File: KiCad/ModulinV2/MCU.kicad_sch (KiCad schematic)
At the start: 36 parts, among them IC1 STM32F401VET6, IC2 STM32F401RET6, J1 USB4105-GF-A, Q1 BC847B,215, Q2 BC847B,215, Q3 BC847B,215, SW1 SW_Push, SW2 SW_Push

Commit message: Added initial power supply schematic and modified MCU components
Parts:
- removed IC1: STM32F401VET6, Modulin:QFP50P1600X1600X160-100N, symbol STM32F401VET6:STM32F401VET6
- removed LED1: 150060VS75000, LEDC1608X80N, symbol 150060VS75000:150060VS75000
- removed Q1, Q2, Q3: BC847B,215, BC847B215, symbol BC847B_215:BC847B,215
- removed R4, R6, R9: 68k, symbol Device:R
- added C83, C84, C85: 100n, symbol Device:C
- added IC31: USBLC6-2SC6, SOT95P280X145-6N, symbol USBLC6-2SC6:USBLC6-2SC6
- added J3: TSW-104-07-G-S, TSW10407GS, symbol TSW-104-07-G-S:TSW-104-07-G-S
- added J4: TSM-103-01-T-DV, TSM-103-YY-ZZZ-DV, symbol TSM-103-01-T-DV:TSM-103-01-T-DV
- added JP5: OLED_PWR, symbol Jumper:SolderJumper_3_Open
- added R118, R119: 10k, symbol Device:R
- added S2: PEC12R-3220F-S0024, PEC12R3220FS0024, symbol PEC12R-3220F-S0024:PEC12R-3220F-S0024
- R3: value 300 -> 10k
- R5: value 130 -> 240
- R7, R8: value 51 -> 240
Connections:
- net ADSR_ENC_A is gone; now on net ENC_A: IC2.14 (PA0)
- net +3.3V: now also R3.1, J4.3, JP5.1 (A), R118.2, S2.2
- net +5V: now also JP5.3 (B)
- net GND: now also C83.2, C84.2, C85.2, IC31.2, J3.1, J4.1, R119.2, S2.C1 (COM), S2.MH1, S2.MH2
- net LED_B: now also R8.2
- net LED_G: now also R7.1
- net LED_R: now also R5.2
- net NRST: now also J4.2
- net SCL: now also J3.3
- net SDA: now also J3.4
- net SWCLK: now also J4.4
- net SWDIO: now also J4.6
- net SWO: now also J4.5
- net USB_DM: now also IC31.1, IC31.6
- net USB_DP: now also IC31.3, IC31.4
- net VBUS: now reaches D1.2 (A), J1.A4 (VBUS), J1.A9 (VBUS), J1.B4 (VBUS), J1.B9 (VBUS)
- net VBUS: now also C83.1, IC31.5; no longer R3.1
- net ENC_A: now reaches R3.2
- net ENC_A: now also C84.1, S2.A1 (CH_A)
- net at R8.1: now also LED2.2
- net at LED2.3: now also R7.2; no longer R7.1
- net ENC_SW: now reaches IC2.16 (PA2)
- net ENC_SW: now also R119.1, S2.1
- net ADSR_ENC_B renamed ENC_B
- net ENC_B: now also C85.1, R118.1, S2.B1 (CH_B)
- net LFO_ENC_A: no longer names the net of IC2.41 (PA8)
- net LFO_ENC_B: no longer names the net of IC2.42 (PA9)
- new net: J3.2, JP5.2 (C)
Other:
- note added: "Debug LED and OLED"
- note added: "Debugger interface"
- note added: "USB interface"
- moved on the sheet: D1, IC2, J1, LED2, R1, R2, R5, R7, R8

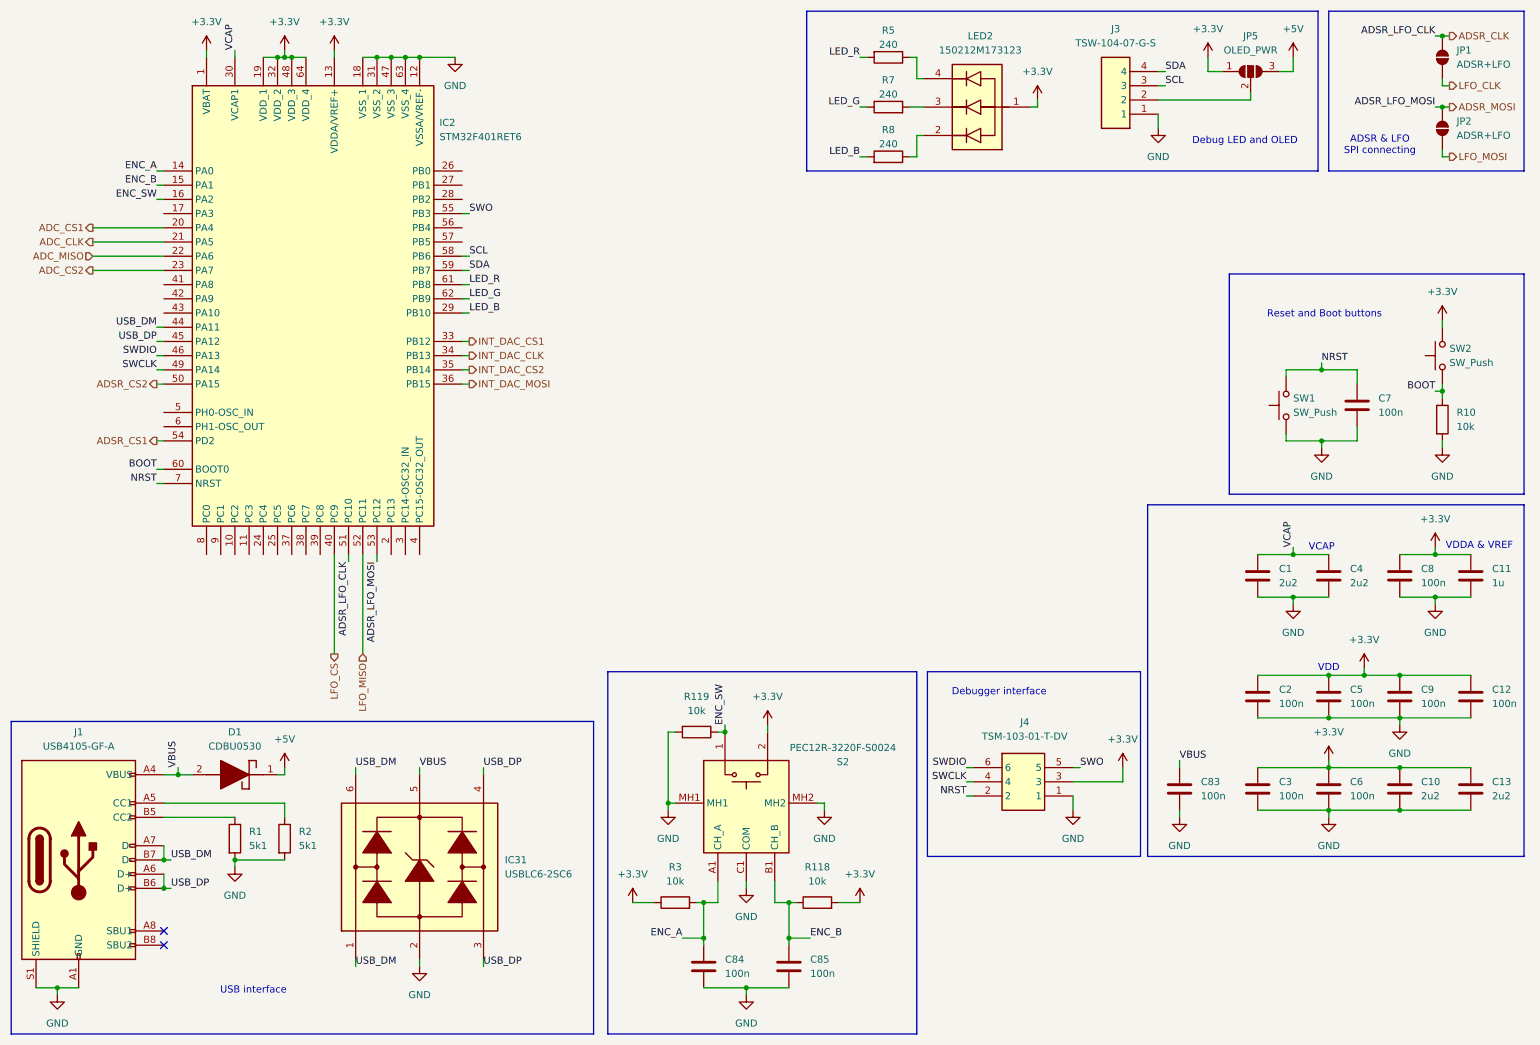
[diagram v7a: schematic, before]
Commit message: Designed ADSR and better tuning schematics with digital/manual capability
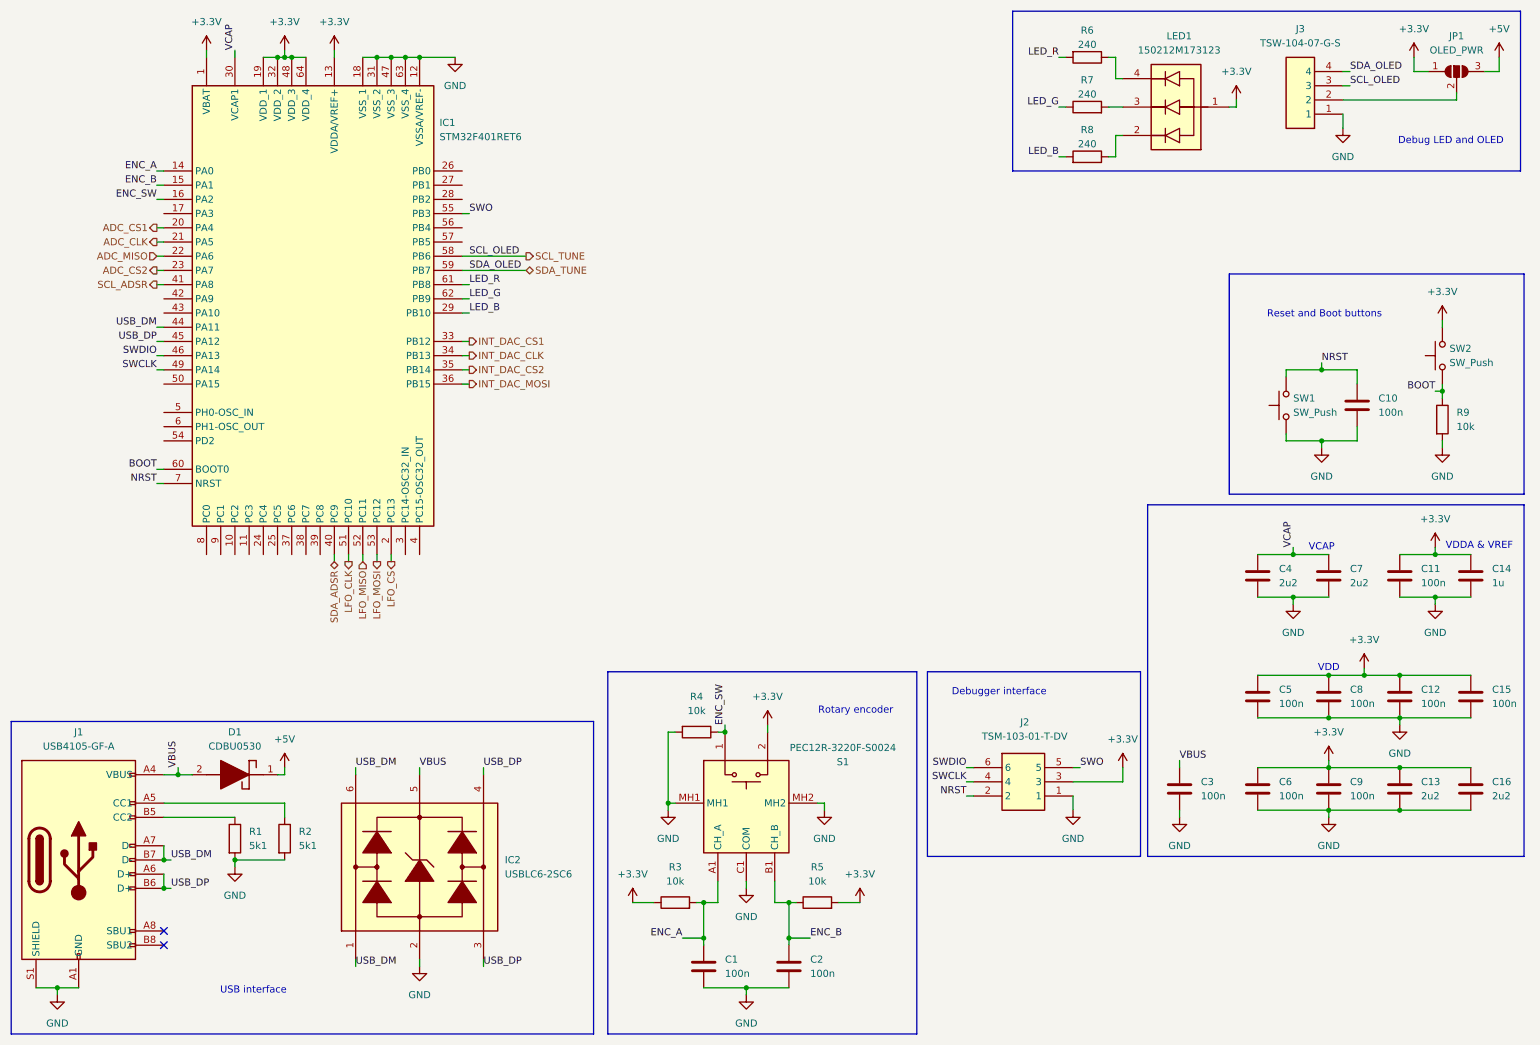
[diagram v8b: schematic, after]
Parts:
- removed JP1, JP2: ADSR+LFO, symbol Jumper:SolderJumper_2_Open
- renumbered C84 to C1, C7 to C10, C8 to C11, C9 to C12, C10 to C13, C11 to C14, C12 to C15, C13 to C16, C85 to C2, C83 to C3, C1 to C4, C2 to C5, C3 to C6, C4 to C7, C5 to C8, C6 to C9, IC2 to IC1, IC31 to IC2, J4 to J2, JP5 to JP1, LED2 to LED1, R119 to R4, R118 to R5, R5 to R6, R10 to R9, S2 to S1
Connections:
- net ADSR_CLK is gone; now on net LFO_CLK: IC1.51 (PC10)
- net ADSR_MOSI is gone; now on net LFO_MOSI: IC1.53 (PC12)
- net LFO_CS: now also IC1.2 (PC13); no longer IC1.40 (PC9)
- net SCL_ADSR: now reaches IC1.41 (PA8)
- net ADSR_CS1: no longer names the net of IC1.54 (PD2)
- net ADSR_CS2: no longer names the net of IC1.50 (PA15)
- net SCL renamed SCL_TUNE
- net SDA renamed SDA_TUNE
- new net SDA_ADSR: IC1.40 (PC9)
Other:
- note added: "Rotary encoder"
- note removed: "ADSR & LFO SPI connecting"
- moved on the sheet: J3, JP1, LED1, R6, R7, R8
